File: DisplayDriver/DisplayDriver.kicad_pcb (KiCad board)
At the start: 2 copper layers, 125 x 75 mm, 50 parts, among them J1 HTSS-108-01-G-D, J2 HEADER-1X14, SW1 (Generic) Lab Kit, U1 ESP32-S3-WROOM-1, U2 74AHCT245, U3 74AHCT245, X2 UJ20-C-H-G-SMT-TR

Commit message: lap to PC
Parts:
- added U4: AMS1117-3.3, Package_TO_SOT_SMD:SOT-223-3_TabPin2, F.Cu at (72.1, 86.3)
- BOOT1: renamed from SW1; footprint DisplayLibrary:SW_PUSH_6mm -> Button_Switch_THT:SW_PUSH_6mm
- C1, C16, C17, C2: footprint DisplayLibrary:C_0603_1608Metric -> Capacitor_SMD:C_0603_1608Metric
- C13, C14, C6, C7, C8: footprint DisplayLibrary:C_0805_2012Metric_Pad1.18x1.45mm_HandSolder -> Capacitor_SMD:C_0805_2012Metric_Pad1.18x1.45mm_HandSolder
- D1, D2, D3: footprint DisplayLibrary:LED_0603_1608Metric -> LED_SMD:LED_0603_1608Metric
- DOWN1, UP1: value TL3330AF260QG -> SW_Push; footprint DisplayLibrary:Molex_KK-254_AE-6410-02A_1x02_P2.54mm_Vertical -> Connector_Molex:Molex_KK-254_AE-6410-02A_1x02_P2.54mm_Vertical
- J2: footprint DisplayLibrary:PinHeader_1x14_P2.54mm_Vertical -> Connector_PinHeader_2.54mm:PinHeader_1x14_P2.54mm_Vertical
- R1, R10, R11, R2, R25, R26, R28, R29, R4, R5, R6, R7: footprint DisplayLibrary:R_0805_2012Metric_Pad1.20x1.40mm_HandSolder -> Resistor_SMD:R_0805_2012Metric_Pad1.20x1.40mm_HandSolder
- R12, R13, R14, R15, R16, R17, R18, R19, R20, R21, R22, R3: footprint DisplayLibrary:R_0603_1608Metric -> Resistor_SMD:R_0603_1608Metric
- RST1: value TL3330AF260QG -> (Generic) Lab Kit; footprint DisplayLibrary:Molex_KK-254_AE-6410-02A_1x02_P2.54mm_Vertical -> Button_Switch_THT:SW_PUSH_6mm
- SJ1: footprint DisplayLibrary:SolderJumper-3_P1.3mm_Open_RoundedPad1.0x1.5mm_NumberLabels -> Jumper:SolderJumper-3_P1.3mm_Open_RoundedPad1.0x1.5mm_NumberLabels
- U1: footprint DisplayLibrary:ESP32-S3-WROOM-1 -> RF_Module:ESP32-S3-WROOM-1
- moved RST1 4.98 mm to (58.7, 60.3), turned to 180 degrees
- moved C6 1.50 mm to (57.7, 48.6)
- moved R2 1.25 mm to (61.2, 48.6)
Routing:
- net /~{RESET}: track 85.6 -> 78.0 mm
- net /UP: track 18.4 -> 20.9 mm
- net 3.3V: track 206.7 -> 204.3 mm
- net GND: track 233.7 -> 231.6 mm
- net Net-(U3-A3): track 55.7 -> 54.8 mm

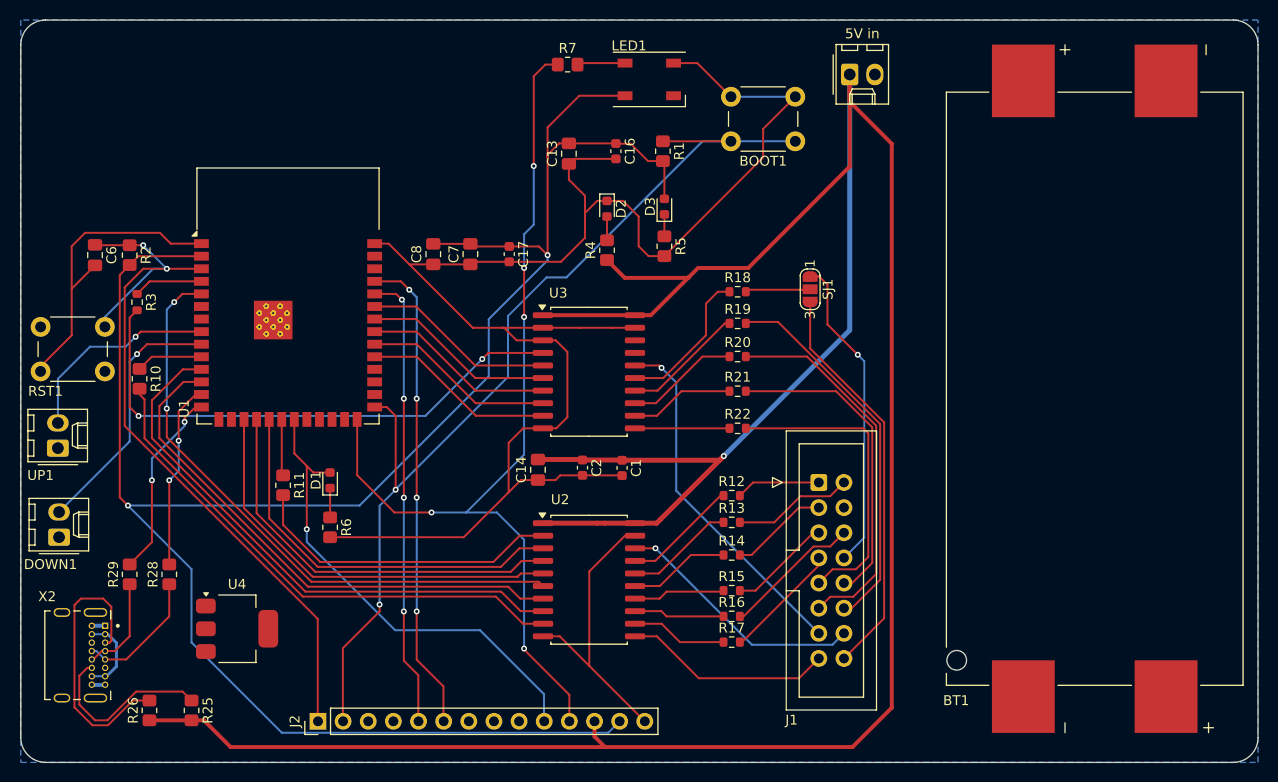
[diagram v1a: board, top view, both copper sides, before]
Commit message: change the ****** shifter footprint
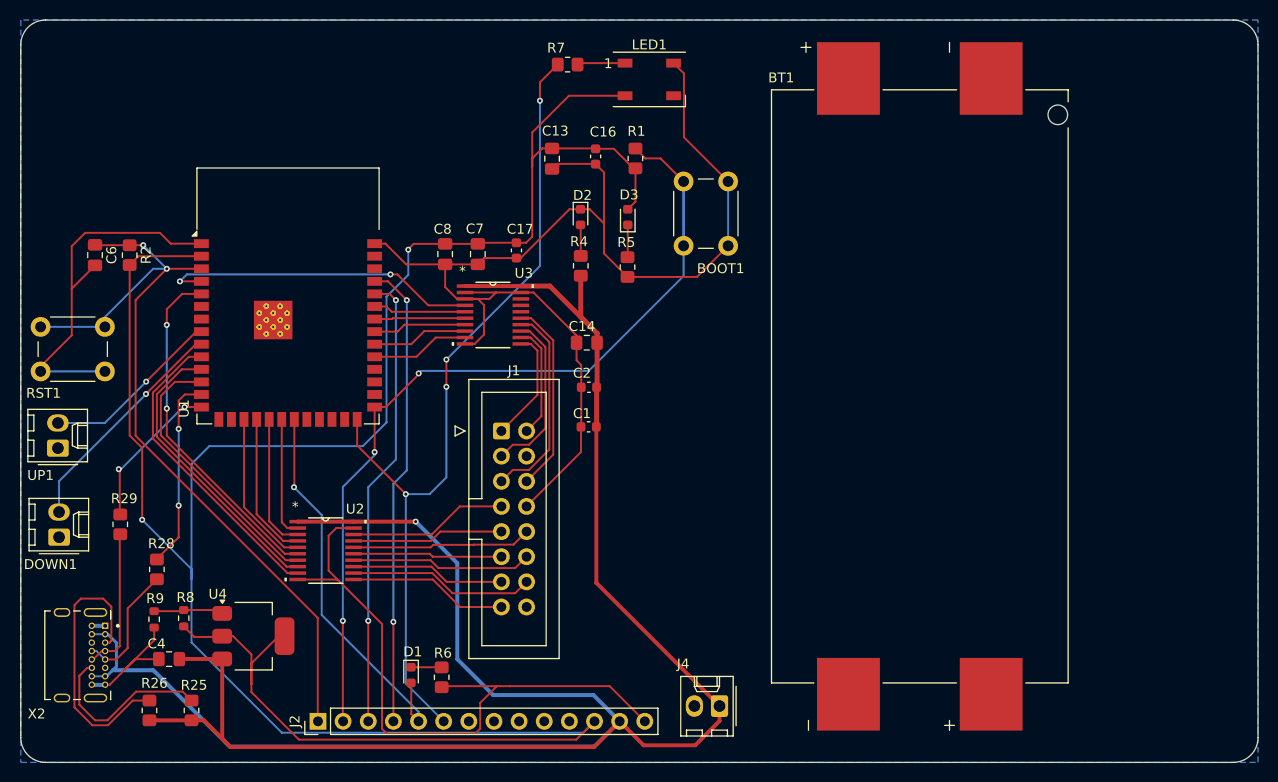
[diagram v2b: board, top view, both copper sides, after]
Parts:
- removed R10, R11: 33, Resistor_SMD:R_0805_2012Metric_Pad1.20x1.40mm_HandSolder
- removed R12, R13, R14, R15, R16, R17, R18, R19, R20, R21, R22: 22, Resistor_SMD:R_0603_1608Metric
- removed R3: 33, Resistor_SMD:R_0603_1608Metric
- removed SJ1: SOLDERJUMPER_2WAY, Jumper:SolderJumper-3_P1.3mm_Open_RoundedPad1.0x1.5mm_NumberLabels
- added C4: C, Capacitor_SMD:C_0805_2012Metric_Pad1.18x1.45mm_HandSolder, F.Cu at (65.2, 89.4)
- added R8: R, Resistor_SMD:R_0603_1608Metric, F.Cu at (66.7, 85.3)
- added R9: R, Resistor_SMD:R_0603_1608Metric, F.Cu at (63.7, 85.4)
- J1: footprint DisplayLibrary:IDC-Header_2x08_P2.54mm_Vertical -> DisplayDriver:IDC-Header_2x08_P2.54mm_Vertical
- J4: renamed from 5V in; value Molex_KK-254_AE-6410-02A_1x02_P2.54mm_Vertical -> Molex; footprint DisplayLibrary:Molex_KK-254_AE-6410-02A_1x02_P2.54mm_Vertical -> Connector_Molex:Molex_KK-254_AE-6410-02A_1x02_P2.54mm_Vertical
- LED1: value WS2812B_3535FULL -> ~; footprint DisplayLibrary:LED_WS2812B_PLCC4_5.0x5.0mm_P3.2mm -> LED_SMD:LED_WS2812B_PLCC4_5.0x5.0mm_P3.2mm
- U2, U3: footprint DisplayLibrary:SOIC-20W_7.5x12.8mm_P1.27mm -> DisplayDriver:PW20
- X2: footprint DisplayLibrary:CUI_UJ20-C-H-G-SMT-TR -> DisplayDriver:CUI_UJ20-C-H-G-SMT-TR
- moved J4 65.1 mm to (120.8, 94.1), turned to 180 degrees
- moved J1 32.5 mm to (98.8, 66.3)
- moved U2 26.8 mm to (81.0, 78.4)
- moved D1 21.3 mm to (89.7, 91.0), turned to -90 degrees
- moved R6 18.9 mm to (92.8, 91.2)
- moved BT1 17.7 mm to (141.1, 61.8), turned to -90 degrees
- moved BOOT1 15.5 mm to (117.2, 47.6), turned to 90 degrees
- moved C14 13.8 mm to (107.4, 57.4), turned to 0 degrees
- moved U3 11.3 mm to (97.9, 54.6)
- moved C2 8.15 mm to (107.6, 61.9), turned to 180 degrees
- moved C1 5.35 mm to (107.6, 65.9), turned to 180 degrees
- moved R29 5.14 mm to (60.3, 75.8)
- moved R5 4.28 mm to (111.5, 49.8)
- moved D3 3.85 mm to (111.5, 44.7)
- moved R4 3.09 mm to (106.8, 49.7)
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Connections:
- J1 pad 08: /M1_E8 -> GND
- J1 pad 16: /M1_E16 -> GND
- J2 pad 10: /D13 -> unconnected-(J2-Pin_10-Pad10)
- J2 pad 11: /NEOPIX -> unconnected-(J2-Pin_11-Pad11)
- J2 pad 12: +5V -> 3.3V
- J2 pad 13: 3.3V -> +5V
- J2 pad 3: unconnected-(J2-Pin_3-Pad3) -> /UART_RX
- J2 pad 4: unconnected-(J2-Pin_4-Pad4) -> /UART_TX
- J2 pad 5: /UART_RX -> /D13
- J2 pad 6: /UART_TX -> /NEOPIX
- U1 pad 11: /B2_3V -> /LAT_3V
- U1 pad 12: /G2_3V -> /CLK_3V
- U1 pad 17: /B1_3V -> /ADDRC_3V
- U1 pad 18: /G1_3V -> /ADDRB_3V
- U1 pad 19: /R1_3V -> /ADDRA_3V
- U1 pad 20: /LAT_3V -> /B2_3V
- U1 pad 31: /ADDRA_3V -> /R1_3V
- U1 pad 32: /ADDRB_3V -> /G1_3V
- U1 pad 33: /ADDRC_3V -> /B1_3V
- U1 pad 34: /ADDRD_3V -> /R2_3V
- U1 pad 35: /ADDRE_3V -> /G2_3V
- U1 pad 4: /CLK_3V -> /ADDRE_3V
- U1 pad 5: /R2_3V -> /ADDRD_3V
- U2 pad 12: Net-(U2-B7) -> /LAT
- U2 pad 13: Net-(U2-B6) -> /CLK
- U2 pad 14: Net-(U2-B5) -> /M1_D
- U2 pad 15: Net-(U2-B4) -> /M1_C
- U2 pad 16: Net-(U2-B3) -> /M1_B
- U2 pad 17: Net-(U2-B2) -> /M1_A
- U2 pad 18: /LAT -> /M1_B2
- U2 pad 2: Net-(U2-A1) -> /B2_3V
- U2 pad 3: /R1_3V -> /ADDRA_3V
- U2 pad 4: /G1_3V -> /ADDRB_3V
- U2 pad 5: /B1_3V -> /ADDRC_3V
- U2 pad 6: /R2_3V -> /ADDRD_3V
- U2 pad 7: /G2_3V -> /CLK_3V
- U2 pad 8: /B2_3V -> /LAT_3V
- U2 pad 9: Net-(U2-A8) -> /OE_3V
- U3 pad 11: Net-(U3-B8) -> /M1_R1
- U3 pad 12: Net-(U3-B7) -> /M1_G1
- U3 pad 13: Net-(U3-B6) -> /M1_B1
- U3 pad 14: Net-(U3-B5) -> /M1_R2
- U3 pad 15: Net-(U3-B4) -> /M1_G2
- U3 pad 16: /CLK -> /M1_E
- U3 pad 4: Net-(U3-A3) -> /ADDRE_3V
- U3 pad 5: /ADDRE_3V -> /G2_3V
- U3 pad 6: /ADDRD_3V -> /R2_3V
- U3 pad 7: /ADDRC_3V -> /B1_3V
- U3 pad 8: /ADDRB_3V -> /G1_3V
- U3 pad 9: /ADDRA_3V -> /R1_3V
- U4 pad 1: GND -> Net-(U4-GND)
- X2 pad A4: Net-(X2-VBUS-PadA4) -> +5V
- X2 pad A9: Net-(X2-VBUS-PadA4) -> +5V
- X2 pad B4: Net-(X2-VBUS-PadA4) -> +5V
- X2 pad B9: Net-(X2-VBUS-PadA4) -> +5V
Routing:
- net Net-(U3-A3): track 54.8 -> 0.00 mm, vias 2 -> 0
- net Net-(U2-A8): track 52.7 -> 0.00 mm
- net /R2_3V: track 61.3 -> 9.17 mm, vias 2 -> 0
- net 3.3V: track 204.3 -> 252.2 mm
- net /G2_3V: track 54.0 -> 9.35 mm
- net /B2_3V: track 56.9 -> 12.3 mm
- net /M1_E16: track 40.8 -> 0.00 mm
- net +5V: track 285.3 -> 249.1 mm
- net /B1_3V: track 42.2 -> 9.42 mm
- net /M1_E8: track 32.1 -> 0.00 mm, vias 1 -> 0
- net Net-(U2-A1): track 31.9 -> 0.00 mm
- net /G1_3V: track 41.3 -> 9.68 mm
- net /R1_3V: track 40.5 -> 10.00 mm
- net /OE_3V: track 6.76 -> 31.3 mm
- net /LAT_3V: track 5.71 -> 29.5 mm
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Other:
- board text removed: "space for regulator"

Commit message: I swear this is the last PCB revision
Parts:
- removed C14: 10uF, Capacitor_SMD:C_0805_2012Metric_Pad1.18x1.45mm_HandSolder
- removed C16, C17: 0.1uF, Capacitor_SMD:C_0603_1608Metric
- removed DOWN1, UP1: SW_Push, Connector_Molex:Molex_KK-254_AE-6410-02A_1x02_P2.54mm_Vertical
- removed the R8 at (66.7, 85.3)
- removed the R9 at (63.7, 85.4)
- added C12: C, DisplayLibrary:C_0805_2012Metric_Pad1.18x1.45mm_HandSolder, F.Cu at (63.8, 91.2)
- added C3: 0.1uF, DisplayLibrary:C_0603_1608Metric, F.Cu at (61.8, 48.3)
- added C5: 0.1uF, DisplayLibrary:C_0603_1608Metric, F.Cu at (96.7, 52.2)
- added C9: 0.1uF, DisplayLibrary:C_0603_1608Metric, F.Cu at (89.5, 84.5)
- added MOL1: CASE_SW, DisplayLibrary:Molex_KK-254_AE-6410-02A_1x02_P2.54mm_Vertical, F.Cu at (54.1, 58.8)
- added MOL2: CASE_SW, DisplayLibrary:Molex_KK-254_AE-6410-02A_1x02_P2.54mm_Vertical, F.Cu at (54.1, 68.0)
- added MOL3: CASE_SW, DisplayLibrary:Molex_KK-254_AE-6410-02A_1x02_P2.54mm_Vertical, F.Cu at (54.1, 77.1)
- BOOT1, RST1: value (Generic) Lab Kit -> Lab Kit; footprint Button_Switch_THT:SW_PUSH_6mm -> DisplayLibrary:SW_PUSH_6mm
- C1: value 0.1uF -> 10uF; footprint Capacitor_SMD:C_0603_1608Metric -> DisplayLibrary:C_0805_2012Metric_Pad1.18x1.45mm_HandSolder
- C13: value 100uF -> C; footprint Capacitor_SMD:C_0805_2012Metric_Pad1.18x1.45mm_HandSolder -> DisplayLibrary:C_0805_2012Metric_Pad1.18x1.45mm_HandSolder
- C2: value 0.1uF -> 1uF; footprint Capacitor_SMD:C_0603_1608Metric -> DisplayLibrary:C_0805_2012Metric_Pad1.18x1.45mm_HandSolder
- C4: value C -> 10uF; footprint Capacitor_SMD:C_0805_2012Metric_Pad1.18x1.45mm_HandSolder -> DisplayLibrary:C_0805_2012Metric_Pad1.18x1.45mm_HandSolder
- C6: value 1uF -> 0.1uF; footprint Capacitor_SMD:C_0805_2012Metric_Pad1.18x1.45mm_HandSolder -> DisplayLibrary:C_0603_1608Metric
- C7: footprint Capacitor_SMD:C_0805_2012Metric_Pad1.18x1.45mm_HandSolder -> DisplayLibrary:C_0805_2012Metric_Pad1.18x1.45mm_HandSolder
- C8: value 10uF -> 100uF; footprint Capacitor_SMD:C_0805_2012Metric_Pad1.18x1.45mm_HandSolder -> DisplayLibrary:C_0805_2012Metric_Pad1.18x1.45mm_HandSolder
- D1, D2, D3: footprint LED_SMD:LED_0603_1608Metric -> DisplayLibrary:LED_0603_1608Metric
- J1: footprint DisplayDriver:IDC-Header_2x08_P2.54mm_Vertical -> DisplayLibrary:IDC-Header_2x08_P2.54mm_Vertical
- J2: footprint Connector_PinHeader_2.54mm:PinHeader_1x14_P2.54mm_Vertical -> DisplayLibrary:PinHeader_1x14_P2.54mm_Vertical
- LED1: footprint LED_SMD:LED_WS2812B_PLCC4_5.0x5.0mm_P3.2mm -> DisplayLibrary:LED_WS2812B_PLCC4_5.0x5.0mm_P3.2mm
- MOL4: renamed from J4; value Molex -> Vin; footprint Connector_Molex:Molex_KK-254_AE-6410-02A_1x02_P2.54mm_Vertical -> DisplayLibrary:Molex_KK-254_AE-6410-02A_1x02_P2.54mm_Vertical
- R1, R2, R4, R5, R6, R7: footprint Resistor_SMD:R_0805_2012Metric_Pad1.20x1.40mm_HandSolder -> DisplayLibrary:R_0805_2012Metric_Pad1.20x1.40mm_HandSolder
- R10: renamed from R26; footprint Resistor_SMD:R_0805_2012Metric_Pad1.20x1.40mm_HandSolder -> DisplayLibrary:R_0805_2012Metric_Pad1.20x1.40mm_HandSolder
- R11: renamed from R25; footprint Resistor_SMD:R_0805_2012Metric_Pad1.20x1.40mm_HandSolder -> DisplayLibrary:R_0805_2012Metric_Pad1.20x1.40mm_HandSolder
- R8: renamed from R28; footprint Resistor_SMD:R_0805_2012Metric_Pad1.20x1.40mm_HandSolder -> DisplayLibrary:R_0805_2012Metric_Pad1.20x1.40mm_HandSolder
- R9: renamed from R29; footprint Resistor_SMD:R_0805_2012Metric_Pad1.20x1.40mm_HandSolder -> DisplayLibrary:R_0805_2012Metric_Pad1.20x1.40mm_HandSolder
- U1: footprint RF_Module:ESP32-S3-WROOM-1 -> DisplayLibrary:ESP32-S3-WROOM-1
- U2, U3: footprint DisplayDriver:PW20 -> DisplayLibrary:PW20
- U4: footprint Package_TO_SOT_SMD:SOT-223-3_TabPin2 -> DisplayLibrary:SOT-223-3_TabPin2
- X2: footprint DisplayDriver:CUI_UJ20-C-H-G-SMT-TR -> DisplayLibrary:CUI_UJ20-C-H-G-SMT-TR
- moved MOL4 65.4 mm to (114.5, 29.1), turned to 0 degrees
- moved C1 56.5 mm to (54.0, 48.0), turned to -90 degrees
- moved D3 56.3 mm to (76.8, 89.0), turned to 180 degrees
- moved LED1 54.0 mm to (96.8, 82.1)
- moved R7 52.9 mm to (88.2, 79.4), turned to -90 degrees
- moved C4 52.9 mm to (105.0, 54.6), turned to 90 degrees
- moved C13 51.8 mm to (65.8, 74.0)
- moved C2 51.5 mm to (58.0, 48.0), turned to -90 degrees
- moved R5 45.9 mm to (78.9, 82.0), turned to 90 degrees
- moved C6 42.6 mm to (97.0, 65.0), turned to 180 degrees
- moved C8 36.7 mm to (85.2, 84.3)
- moved C7 36.4 mm to (65.8, 68.2), turned to -90 degrees
- moved R2 36.2 mm to (75.0, 82.0)
- moved RST1 25.0 mm to (77.8, 76.4)
- moved BOOT1 21.2 mm to (108.1, 28.4), turned to -90 degrees
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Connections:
- BT1 pad N1: unconnected-(BT1-PadN1) -> Net-(BT1-PadN1)
- BT1 pad N2: unconnected-(BT1-PadN2) -> GND
- BT1 pad P2: unconnected-(BT1-PadP2) -> Net-(BT1-PadN1)
- C1 pad 1: +5V -> GND
- C1 pad 2: GND -> 3.3V
- C13 pad 1: GND -> 3.3V
- C13 pad 2: 3.3V -> GND
- C2 pad 1: +5V -> GND
- C2 pad 2: GND -> 3.3V
- C4 pad 1: +5V -> GND
- C4 pad 2: GND -> +5V
- C6 pad 1: /~{RESET} -> +5V
- C7 pad 1: GND -> /~{RESET}
- C7 pad 2: 3.3V -> GND
- D1 pad 2: /D13 -> /D9
- J2 pad 5: /D13 -> /D9
- U1 pad 10: /OE_3V -> /A2
- U1 pad 11: /LAT_3V -> unconnected-(U1-IO18-Pad11)
- U1 pad 12: /CLK_3V -> unconnected-(U1-IO8-Pad12)
- U1 pad 17: /ADDRC_3V -> /D9
- U1 pad 18: /ADDRB_3V -> /OE_3V
- U1 pad 19: /ADDRA_3V -> /CLK_3V
- U1 pad 20: /B2_3V -> /LAT_3V
- U1 pad 21: /D13 -> /ADDRC_3V
- U1 pad 22: unconnected-(U1-IO14-Pad22) -> /ADDRD_3V
- U1 pad 23: unconnected-(U1-IO21-Pad23) -> /ADDRA_3V
- U1 pad 24: unconnected-(U1-IO47-Pad24) -> /ADDRB_3V
- U1 pad 25: unconnected-(U1-IO48-Pad25) -> /B2_3V
- U1 pad 31: /R1_3V -> /R2_3V
- U1 pad 32: /G1_3V -> /G2_3V
- U1 pad 34: /R2_3V -> /R1_3V
- U1 pad 35: /G2_3V -> /G1_3V
- U1 pad 4: /ADDRE_3V -> unconnected-(U1-IO4-Pad4)
- U1 pad 5: /ADDRD_3V -> unconnected-(U1-IO5-Pad5)
- U1 pad 8: /UP -> /A0
- U1 pad 9: /DOWN -> /A1
- U2 pad 12: /LAT -> /CLK
- U2 pad 13: /CLK -> /LAT
- U2 pad 14: /M1_D -> /M1_C
- U2 pad 15: /M1_C -> /M1_D
- U2 pad 16: /M1_B -> /M1_A
- U2 pad 17: /M1_A -> /M1_B
- U2 pad 3: /ADDRA_3V -> /ADDRB_3V
- U2 pad 4: /ADDRB_3V -> /ADDRA_3V
- U2 pad 5: /ADDRC_3V -> /ADDRD_3V
- U2 pad 6: /ADDRD_3V -> /ADDRC_3V
- U2 pad 7: /CLK_3V -> /LAT_3V
- U2 pad 8: /LAT_3V -> /CLK_3V
- U3 pad 11: /M1_R1 -> /M1_R2
- U3 pad 12: /M1_G1 -> /M1_G2
- U3 pad 14: /M1_R2 -> /M1_R1
- U3 pad 15: /M1_G2 -> /M1_G1
- U3 pad 16: /M1_E -> unconnected-(U3-B3-Pad16)
- U3 pad 4: /ADDRE_3V -> GND
- U3 pad 5: /G2_3V -> /G1_3V
- U3 pad 6: /R2_3V -> /R1_3V
- U3 pad 8: /G1_3V -> /G2_3V
- U3 pad 9: /R1_3V -> /R2_3V
- U4 pad 1: Net-(U4-GND) -> GND
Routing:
- net 3.3V: track 252.2 -> 183.0 mm, vias 2 -> 0
- net /NEOPIX: track 85.4 -> 36.1 mm, vias 4 -> 3
- net /D9: track 0.00 -> 45.5 mm, vias 0 -> 1
- net /D13: track 40.0 -> 0.00 mm, vias 1 -> 0
- net /ADDRE_3V: track 32.6 -> 0.00 mm, vias 2 -> 0
- net /A2: track 0.00 -> 25.1 mm, vias 0 -> 1
- net /DOWN: track 23.3 -> 0.00 mm, vias 1 -> 0
- net GND: track 243.8 -> 224.8 mm
- net /UP: track 18.3 -> 0.00 mm, vias 1 -> 0
- net /ADDRD_3V: track 35.1 -> 17.4 mm, vias 2 -> 0
- net /A1: track 0.00 -> 17.6 mm, vias 0 -> 1
- net /A0: track 0.00 -> 14.5 mm, vias 0 -> 1
- net Net-(BT1-PadN1): track 0.00 -> 14.4 mm
- net /~{RESET}: track 82.2 -> 69.9 mm, vias 2 -> 0
- net /LAT_3V: track 29.5 -> 20.4 mm
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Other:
- board size 125 x 75 mm -> 100 x 75 mm

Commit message: e
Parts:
- BOOT1, RST1: footprint DisplayLibrary:SW_PUSH_6mm -> Button_Switch_THT:SW_PUSH_6mm
- C1, C12, C13, C2, C4, C7, C8: footprint DisplayLibrary:C_0805_2012Metric_Pad1.18x1.45mm_HandSolder -> Capacitor_SMD:C_0805_2012Metric_Pad1.18x1.45mm_HandSolder
- C3, C5, C6, C9: footprint DisplayLibrary:C_0603_1608Metric -> Capacitor_SMD:C_0603_1608Metric
- D1, D2, D3: footprint DisplayLibrary:LED_0603_1608Metric -> LED_SMD:LED_0603_1608Metric
- J1: footprint DisplayLibrary:IDC-Header_2x08_P2.54mm_Vertical -> DisplayDriver:IDC-Header_2x08_P2.54mm_Vertical
- J2: footprint DisplayLibrary:PinHeader_1x14_P2.54mm_Vertical -> Connector_PinHeader_2.54mm:PinHeader_1x14_P2.54mm_Vertical
- LED1: footprint DisplayLibrary:LED_WS2812B_PLCC4_5.0x5.0mm_P3.2mm -> LED_SMD:LED_WS2812B_PLCC4_5.0x5.0mm_P3.2mm
- MOL1, MOL2, MOL3, MOL4: footprint DisplayLibrary:Molex_KK-254_AE-6410-02A_1x02_P2.54mm_Vertical -> Connector_Molex:Molex_KK-254_AE-6410-02A_1x02_P2.54mm_Vertical
- R1, R10, R11, R2, R4, R5, R6, R7, R8, R9: footprint DisplayLibrary:R_0805_2012Metric_Pad1.20x1.40mm_HandSolder -> Resistor_SMD:R_0805_2012Metric_Pad1.20x1.40mm_HandSolder
- U1: footprint DisplayLibrary:ESP32-S3-WROOM-1 -> RF_Module:ESP32-S3-WROOM-1
- U2, U3: footprint DisplayLibrary:PW20 -> DisplayDriver:PW20
- U4: footprint DisplayLibrary:SOT-223-3_TabPin2 -> Package_TO_SOT_SMD:SOT-223-3_TabPin2
- X2: footprint DisplayLibrary:CUI_UJ20-C-H-G-SMT-TR -> DisplayDriver:CUI_UJ20-C-H-G-SMT-TR
- moved C8 0.60 mm to (84.6, 84.3)
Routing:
- net GND: track 224.8 -> 225.4 mm

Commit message: bill of mat.
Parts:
- renumbered R11 to R10, R6 to R3, R7 to R6, R8 to R7, R9 to R8, R10 to R9
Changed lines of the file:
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@@
 		(descr "Resistor SMD 0805 (2012 Metric), square (rectangular) end terminal, IPC_7351 nominal with elongated pad for handsoldering. (Body size source: IPC-SM-782 page 72, https://www.pcb-3d.com/wordpress/wp-content/uploads/ipc-sm-782a_amendment_1_and_2.pdf), generated with kicad-footprint-generator")
 		(tags "resistor handsolder")
-		(property "Reference" "R7"
+		(property "Reference" "R6"
 			(at -1.25 -2 0)
 			(layer "F.SilkS")
@@
 		(descr "Resistor SMD 0805 (2012 Metric), square (rectangular) end terminal, IPC_7351 nominal with elongated pad for handsoldering. (Body size source: IPC-SM-782 page 72, https://www.pcb-3d.com/wordpress/wp-content/uploads/ipc-sm-782a_amendment_1_and_2.pdf), generated with kicad-footprint-generator")
 		(tags "resistor handsolder")
-		(property "Reference" "R11"
+		(property "Reference" "R10"
 			(at 1.3 2.45 180)
 			(layer "F.SilkS")
@@
 		(descr "Resistor SMD 0805 (2012 Metric), square (rectangular) end terminal, IPC_7351 nominal with elongated pad for handsoldering. (Body size source: IPC-SM-782 page 72, https://www.pcb-3d.com/wordpress/wp-content/uploads/ipc-sm-782a_amendment_1_and_2.pdf), generated with kicad-footprint-generator")
 		(tags "resistor handsolder")
-		(property "Reference" "R10"
+		(property "Reference" "R9"
 			(at -1.28 -2.6 0)
 			(layer "F.SilkS")
@@
 		(descr "Resistor SMD 0805 (2012 Metric), square (rectangular) end terminal, IPC_7351 nominal with elongated pad for handsoldering. (Body size source: IPC-SM-782 page 72, https://www.pcb-3d.com/wordpress/wp-content/uploads/ipc-sm-782a_amendment_1_and_2.pdf), generated with kicad-footprint-generator")
 		(tags "resistor handsolder")
-		(property "Reference" "R8"
+		(property "Reference" "R7"
 			(at 1.2 1.9 180)
 			(layer "F.SilkS")
@@
 		(descr "Resistor SMD 0805 (2012 Metric), square (rectangular) end terminal, IPC_7351 nominal with elongated pad for handsoldering. (Body size source: IPC-SM-782 page 72, https://www.pcb-3d.com/wordpress/wp-content/uploads/ipc-sm-782a_amendment_1_and_2.pdf), generated with kicad-footprint-generator")
 		(tags "resistor handsolder")
-		(property "Reference" "R6"
+		(property "Reference" "R3"
 			(at 1.2 2 0)
 			(layer "F.SilkS")
@@
 		(descr "Resistor SMD 0805 (2012 Metric), square (rectangular) end terminal, IPC_7351 nominal with elongated pad for handsoldering. (Body size source: IPC-SM-782 page 72, https://www.pcb-3d.com/wordpress/wp-content/uploads/ipc-sm-782a_amendment_1_and_2.pdf), generated with kicad-footprint-generator")
 		(tags "resistor handsolder")
-		(property "Reference" "R9"
+		(property "Reference" "R8"
 			(at 1.3 2 180)
 			(layer "F.SilkS")
@@
 		)
 		(property "Value" "UJ20-C-H-G-SMT-TR"
-			(at 0.025 1.4 270)
+			(at 0.025 1.4 -90)
 			(layer "F.Fab")
 			(effects

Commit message: pcb review prep
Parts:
- moved R3 1.20 mm to (98.4, 88.0)
- moved D1 0.91 mm to (94.0, 89.9)
- moved C8 0.60 mm to (85.2, 84.3)
- moved R6 0.50 mm to (87.7, 79.4)
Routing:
- net /BOOT0: track 95.1 -> 114.7 mm, vias 3 -> 1
- net GND: track 225.4 -> 223.7 mm
- net /NEOPIX: track 36.1 -> 37.5 mm
- net /D9: track 45.5 -> 46.1 mm
- net Net-(LED1-DI): track 6.17 -> 6.67 mm

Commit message: pre-procurement
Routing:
- net GND: track 223.7 -> 26.6 mm
- net +5V: track 251.2 -> 265.3 mm
- net /CC1B: track 31.5 -> 38.9 mm
- net 3.3V: track 182.9 -> 182.3 mm
- added copper zone on F.Cu, net GND
